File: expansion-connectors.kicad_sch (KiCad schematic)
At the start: 7 parts, among them J10 LSHM-130-01-L-RH-A-S-K-TR

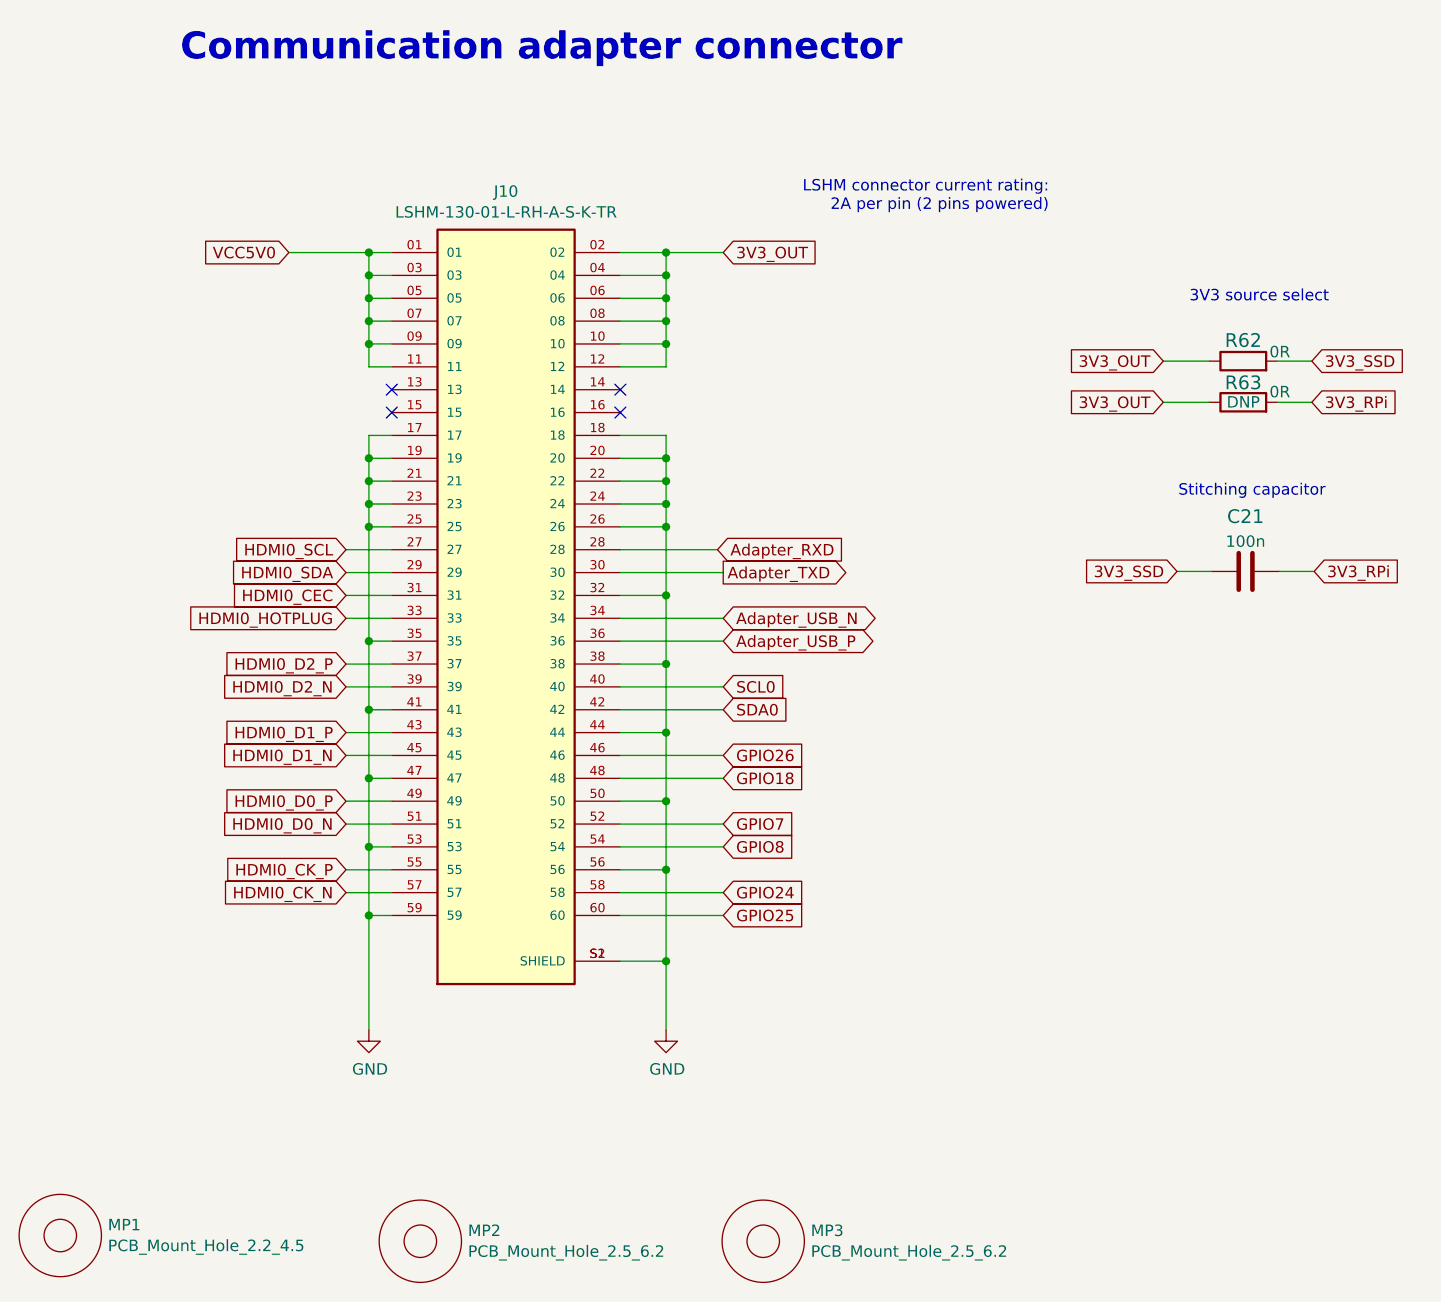
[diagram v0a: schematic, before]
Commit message: Update LSHM-130-01-L-RH-A-S-K-TR symbol and footprint
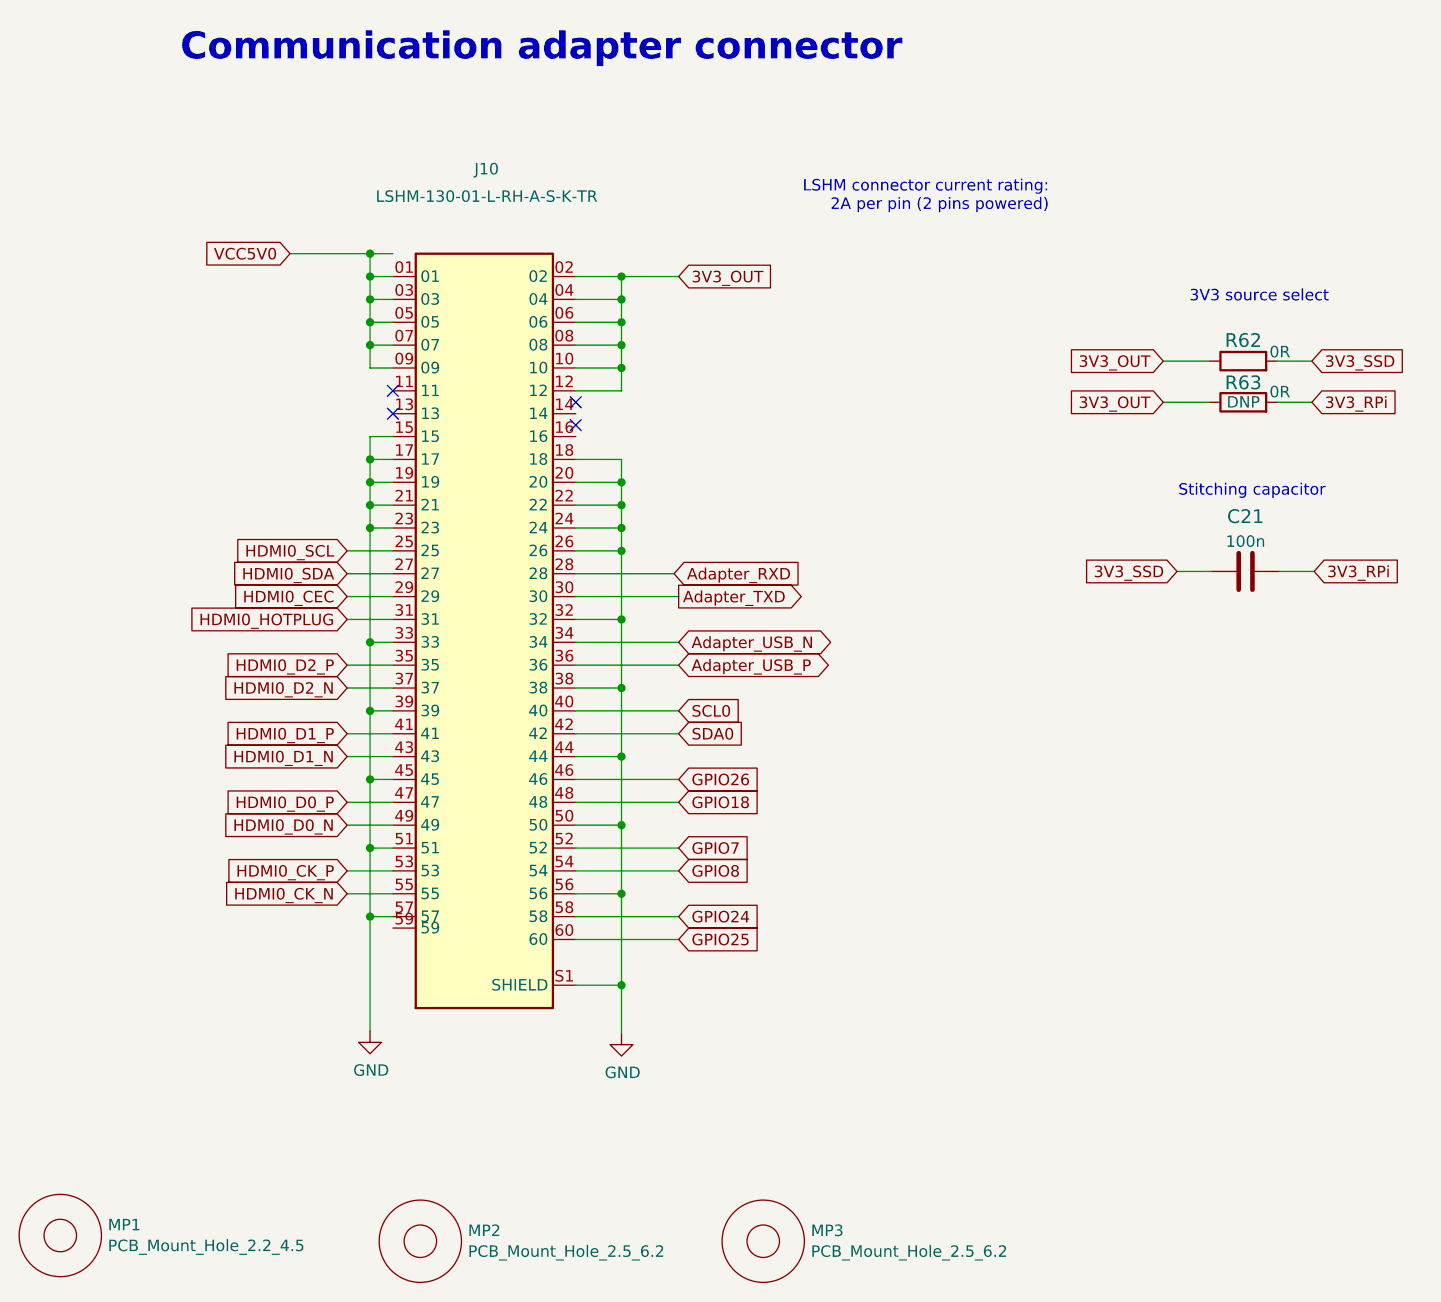
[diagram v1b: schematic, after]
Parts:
- J10: footprint scalenode-cm4-baseboard-footprints:SAMTEC_LSHM-130-01-XXX-RH-A-S-K-XX -> antmicro-footprints:SAMTEC_LSHM-130-01-XXX-RH-A-S-K-XX; symbol scalenode-cm4-baseboard:LSHM-130-01-L-RH-A-S-K-TR -> antmicroB2bConnectors:LSHM-130-01-L-RH-A-S-K-TR; Author (none) -> Antmicro; License (none) -> Apache-2.0; Manufacturer (none) -> Samtec
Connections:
- net GND: now also J10.15, J10.33, J10.39, J10.45, J10.51, J10.57; no longer J10.25, J10.35, J10.41, J10.47, J10.53, J10.59
- net HDMI0_CEC: now also J10.29; no longer J10.31
- net HDMI0_CK_N: now also J10.55; no longer J10.57
- net HDMI0_CK_P: now also J10.53; no longer J10.55
- net HDMI0_D0_N: now also J10.49; no longer J10.51
- net HDMI0_D0_P: now also J10.47; no longer J10.49
- net HDMI0_D1_N: now also J10.43; no longer J10.45
- net HDMI0_D1_P: now also J10.41; no longer J10.43
- net HDMI0_D2_N: now also J10.37; no longer J10.39
- net HDMI0_D2_P: now also J10.35; no longer J10.37
- net HDMI0_HOTPLUG: now also J10.31; no longer J10.33
- net HDMI0_SCL: now also J10.25; no longer J10.27
- net HDMI0_SDA: now also J10.27; no longer J10.29
- net VCC5V0: no longer J10.11

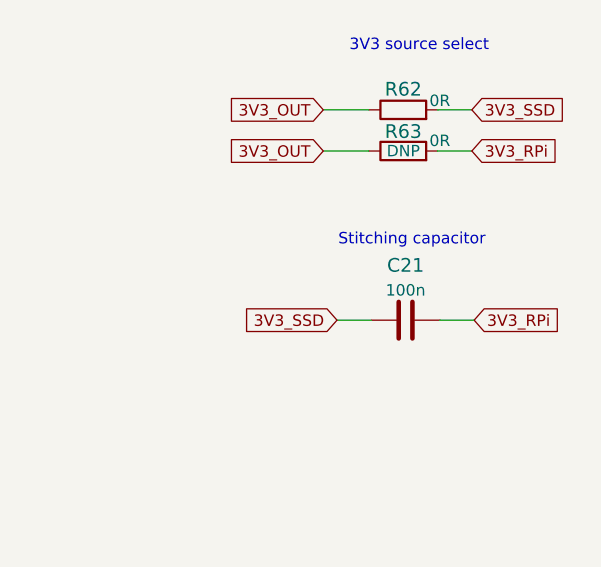
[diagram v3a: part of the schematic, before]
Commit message: Update C13, C17, C21, C37, C51, C54, C55, C56 symbol and footprint
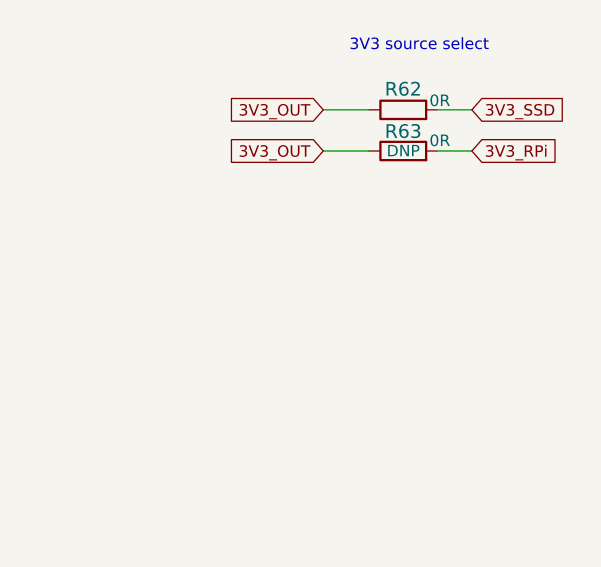
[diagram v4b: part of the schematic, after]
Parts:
- removed C21: C_100n_0402, scalenode-cm4-baseboard-footprints:0402-cap, symbol scalenode-cm4-baseboard:C_100n_0402
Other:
- note removed: "Stitching capacitor"
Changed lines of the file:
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@@
-    (stroke (width 0) (type default) (color 0 0 0 0))
-  )
-  (wire (pts (xy 263.144 122.428) (xy 259.334 122.428))
     (stroke (width 0) (type default) (color 0 0 0 0))
   )
@@
   )
   (wire (pts (xy 172.212 127.762) (xy 167.132 127.762))
-    (stroke (width 0) (type default) (color 0 0 0 0))
-  )
-  (wire (pts (xy 270.764 122.428) (xy 274.574 122.428))
     (stroke (width 0) (type default) (color 0 0 0 0))
   )
@@
     (effects (font (size 1.27 1.27)) (justify right bottom))
   )
-  (text "Stitching capacitor" (at 275.844 114.3 180)
-    (effects (font (size 1.27 1.27)) (justify right bottom))
-  )
   (text "Communication adapter connector" (at 148.59 66.04 0)
     (effects (font (size 2.9972 2.9972) (thickness 0.5994) bold) (justify left bottom))
@@
     )
   )
-  (global_label "3V3_SSD" (shape input) (at 259.334 122.428 180) (fields_autoplaced)
-    (effects (font (size 1.27 1.27)) (justify right))
-    (property "Intersheet References" "${INTERSHEET_REFS}" (id 0) (at 534.289 220.853 0)
-      (effects (font (size 1.27 1.27)) hide)
-    )
-  )
   (global_label "HDMI0_SDA" (shape input) (at 167.132 122.682 180) (fields_autoplaced)
     (effects (font (size 1.27 1.27)) (justify right))
@@
     (effects (font (size 1.27 1.27)) (justify right))
     (property "Intersheet References" "${INTERSHEET_REFS}" (id 0) (at 0.127 0.127 0)
-      (effects (font (size 1.27 1.27)) hide)
-    )
-  )
-  (global_label "3V3_RPi" (shape input) (at 274.574 122.428 0) (fields_autoplaced)
-    (effects (font (size 1.27 1.27)) (justify left))
-    (property "Intersheet References" "${INTERSHEET_REFS}" (id 0) (at -2.921 19.558 0)
       (effects (font (size 1.27 1.27)) hide)
     )
@@
     (pin "1")
   )
-  (symbol (lib_id "scalenode-cm4-baseboard:C_100n_0402") (at 266.954 122.428 90) (unit 1)
-    (in_bom yes) (on_board yes) (fields_autoplaced)
-    (property "Reference" "C21" (id 0) (at 266.954 116.3411 90)
-      (effects (font (size 1.524 1.524)))
-    )
-    (property "Value" "C_100n_0402" (id 1) (at 270.764 122.428 0)
-      (effects (font (size 1.524 1.524)) hide)
-    )
-    (property "Footprint" "scalenode-cm4-baseboard-footprints:0402-cap" (id 2) (at 261.874 117.348 0)
-      (effects (font (size 1.524 1.524)) (justify left) hide)
-    )
-    (property "Datasheet" "" (id 3) (at 266.954 122.428 0)
-      (effects (font (size 1.27 1.27)) hide)
-    )
-    (property "Manufacturer" "Walsin" (id 4) (at 256.794 117.348 0)
-      (effects (font (size 1.524 1.524)) (justify left) hide)
-    )
-    (property "MPN" "0402X104K6R3CT" (id 5) (at 259.334 117.348 0)
-      (effects (font (size 1.524 1.524)) (justify left) hide)
-    )
-    (property "Val" "100n" (id 6) (at 266.954 119.1062 90))
-    (pin "1")
-    (pin "2")
-  )
 )

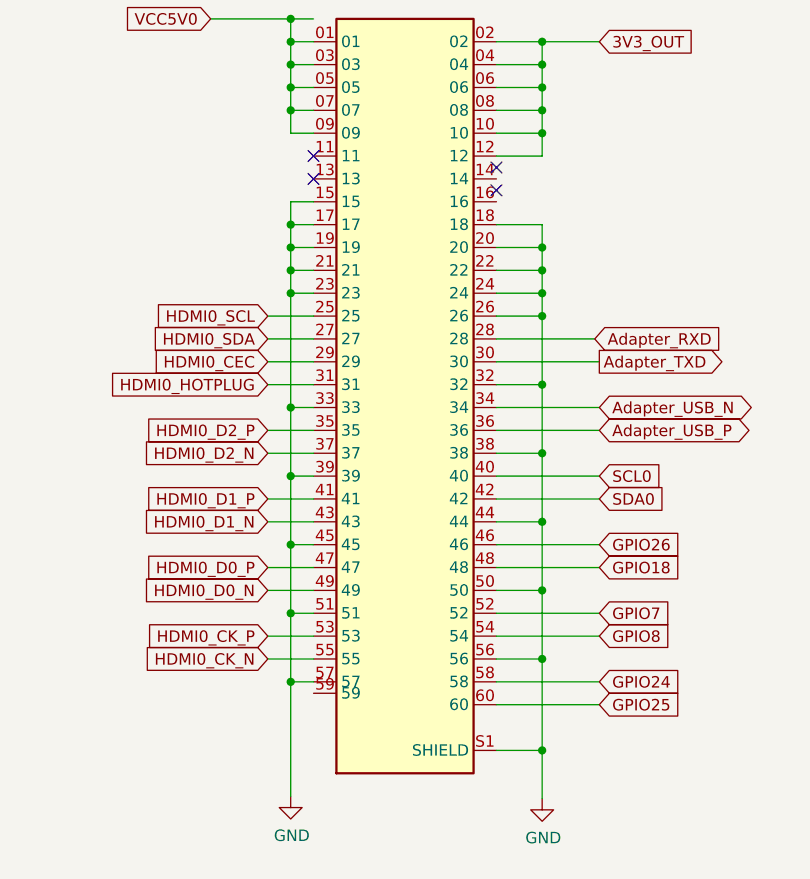
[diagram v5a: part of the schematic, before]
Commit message: Update C26, C28, C29, C32 symbol
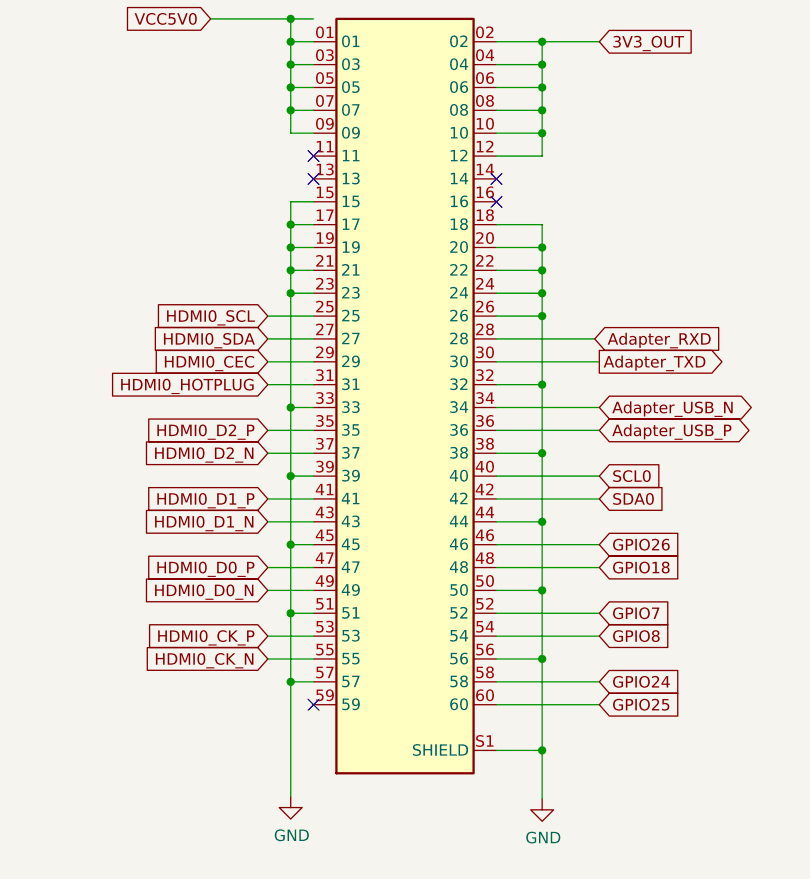
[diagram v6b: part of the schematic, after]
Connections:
- no-connect marks 4 -> 5
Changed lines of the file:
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@@
   (junction (at 169.672 112.522) (diameter 0) (color 0 0 0 0)
   )
-  (no_connect (at 192.532 103.632))
+  (no_connect (at 172.212 163.322))
+  (no_connect (at 192.532 104.902))
   (no_connect (at 172.212 102.362))
   (no_connect (at 172.212 104.902))
-  (no_connect (at 192.532 106.172))
+  (no_connect (at 192.532 107.442))
   (wire (pts (xy 262.89 99.06) (xy 257.81 99.06))
     (stroke (width 0) (type default) (color 0 0 0 0))

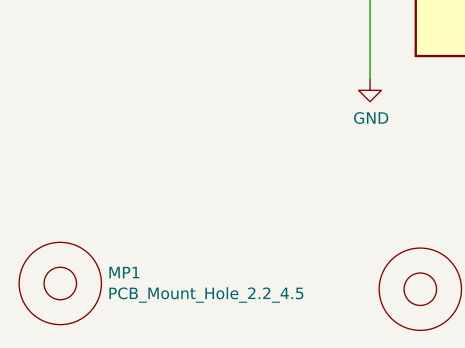
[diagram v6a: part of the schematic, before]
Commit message: Update MP1 symbol and footprint
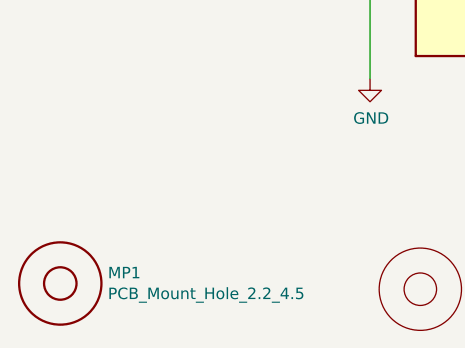
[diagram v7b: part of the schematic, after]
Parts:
- MP1: footprint scalenode-cm4-baseboard-footprints:mounting-hole-2.2mm -> antmicro-footprints:mounting-hole-2.2mm; symbol scalenode-cm4-baseboard:PCB_Mount_Hole_2.2_4.5 -> antmicroMechanicalParts:PCB_Mount_Hole_2.2_4.5; Author (none) -> Antmicro; License (none) -> Apache-2.0; Manufacturer (none) -> None
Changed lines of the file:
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@@
     )
   )
-  (symbol (lib_id "scalenode-cm4-baseboard:PCB_Mount_Hole_2.2_4.5") (at 135.255 196.215 0) (unit 1)
+  (symbol (lib_id "antmicroMechanicalParts:PCB_Mount_Hole_2.2_4.5") (at 135.255 196.215 0) (unit 1)
     (in_bom yes) (on_board yes)
     (property "Reference" "MP1" (id 0) (at 140.5382 195.0466 0)
@@
       (effects (font (size 1.27 1.27)) (justify left))
     )
-    (property "Footprint" "scalenode-cm4-baseboard-footprints:mounting-hole-2.2mm" (id 2) (at 155.575 178.435 0)
-      (effects (font (size 1.27 1.27)) hide)
+    (property "Footprint" "antmicro-footprints:mounting-hole-2.2mm" (id 2) (at 153.035 203.835 0)
+      (effects (font (size 1.27 1.27) (thickness 0.15)) (justify left bottom) hide)
     )
-    (property "Datasheet" "" (id 3) (at 159.385 175.895 0)
-      (effects (font (size 1.27 1.27)) hide)
+    (property "Datasheet" "" (id 3) (at 153.035 206.375 0)
+      (effects (font (size 1.27 1.27) (thickness 0.15)) (justify left bottom) hide)
+    )
+    (property "Manufacturer" "None" (id 4) (at 153.035 206.375 0)
+      (effects (font (size 1.27 1.27) (thickness 0.15)) (justify left bottom) hide)
+    )
+    (property "Author" "Antmicro" (id 5) (at 153.035 208.915 0)
+      (effects (font (size 1.27 1.27) (thickness 0.15)) (justify left bottom) hide)
+    )
+    (property "License" "Apache-2.0" (id 6) (at 153.035 211.455 0)
+      (effects (font (size 1.27 1.27) (thickness 0.15)) (justify left bottom) hide)
     )
   )
